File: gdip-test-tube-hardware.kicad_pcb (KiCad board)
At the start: 2 copper layers, 76.2 x 58.5 mm, 68 parts, among them J1 USB_B, J2 USB_B, J3 Screw_Terminal_01x02, J6 Screw_Terminal_01x02, Q1 BC818, Q2 BC818, Q3 BC818, SW1 SW_Push, SW2 SW_Push, U1 ESP32-S3-WROOM-1-N16R2, U2 AMS1117-3.3, U3 CP2102N-Axx-xQFN28, U4 USBLC6-2SC6, U5 USBLC6-2SC6, U6 74LVC2G00, U7 HDSP-7401, U8 74AHC595

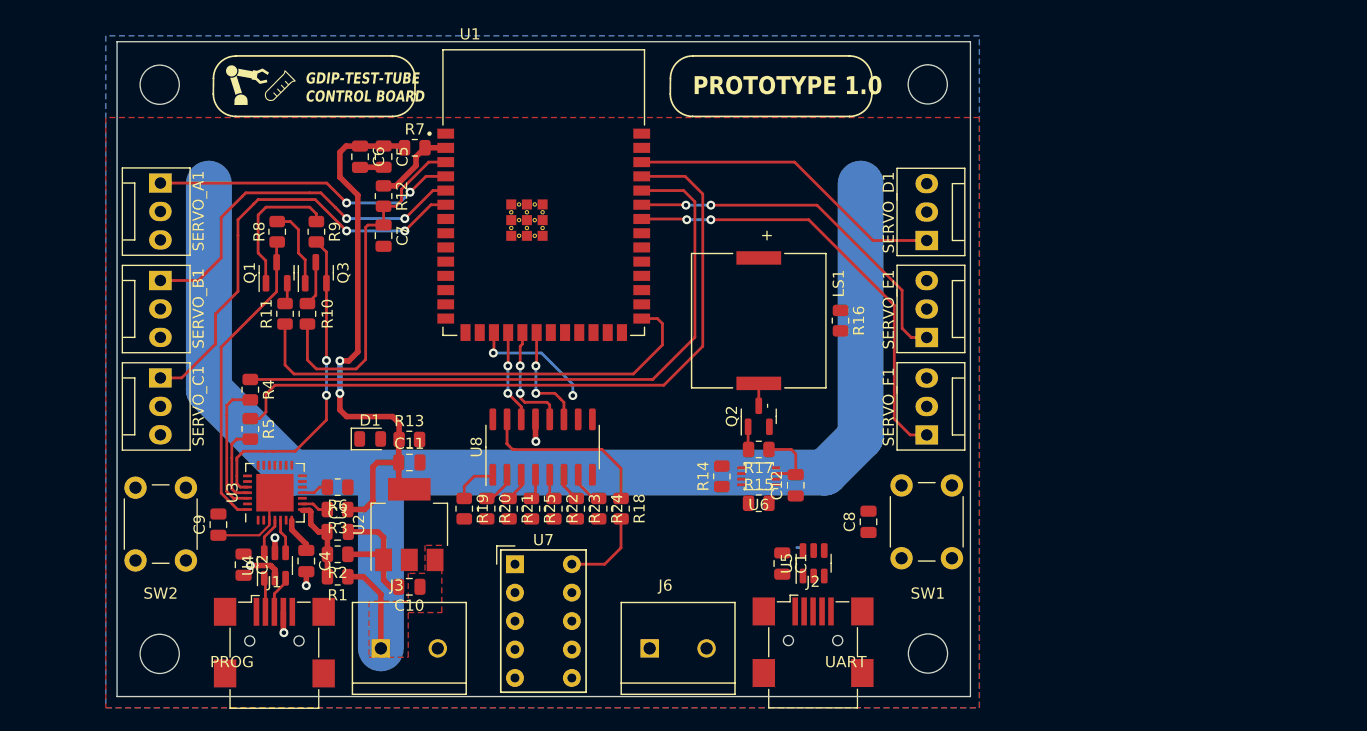
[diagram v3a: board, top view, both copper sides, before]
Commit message: Finished first layout added load switch for led saftey circuit,changed 47uF cap footprint. Also added extra pin headers for USB, Voltages & Gnd on board and extra GPIOs.
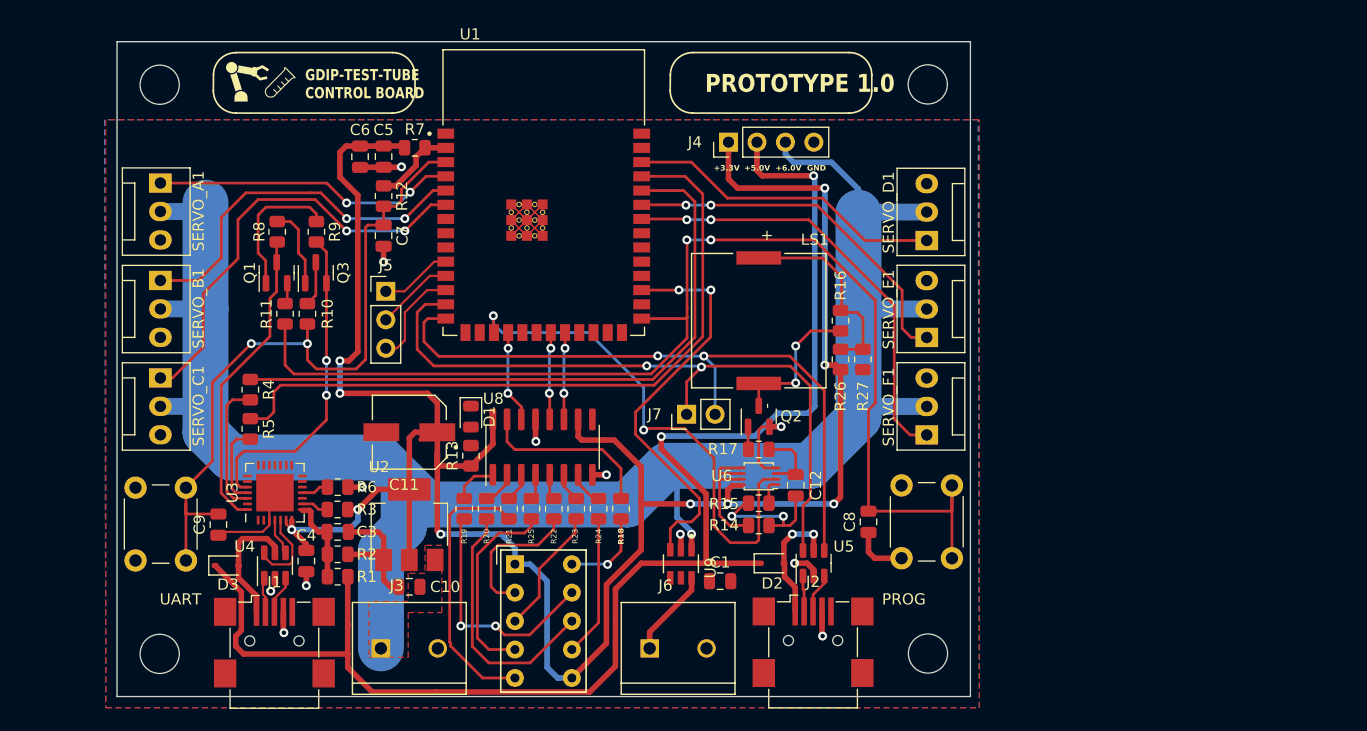
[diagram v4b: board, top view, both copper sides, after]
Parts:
- removed C2: 100nF, Capacitor_SMD:C_0805_2012Metric
- added D2: 1N5819WS, Diode_SMD:D_SOD-323, F.Cu at (158.5, 126.1)
- added D3: 1N5819WS, Diode_SMD:D_SOD-323, F.Cu at (109.8, 126.3)
- added J4: Conn_01x04, Connector_PinHeader_2.54mm:PinHeader_1x04_P2.54mm_Vertical, F.Cu at (154.6, 88.5)
- added J5: Conn_01x03, Connector_PinHeader_2.54mm:PinHeader_1x03_P2.54mm_Vertical, F.Cu at (124.0, 101.8)
- added J7: Conn_01x02, Connector_PinHeader_2.54mm:PinHeader_1x02_P2.54mm_Vertical, F.Cu at (150.9, 112.8)
- added R26: 4.7k, Resistor_SMD:R_0805_2012Metric, F.Cu at (164.6, 107.9)
- added R27: 3.9k, Resistor_SMD:R_0805_2012Metric, F.Cu at (166.6, 107.9)
- added U9: TPS22810DBVT, gdip-test-tube:SOT95P280X145-6N, F.Cu at (150.3, 126.1)
- C1: value 100nF -> 1uF
- C11: footprint Capacitor_SMD:C_0805_2012Metric -> gdip-test-tube:CAP_EEEHA1H470XP
- D1: value LED -> MCUPWR
- moved D1 9.22 mm to (131.6, 113.0), turned to -90 degrees
- moved C1 5.77 mm to (153.8, 127.7), turned to 0 degrees
- moved R13 5.69 mm to (131.6, 116.5), turned to 90 degrees
- moved R14 5.49 mm to (157.3, 122.7), turned to 180 degrees
- moved C11 2.70 mm to (126.1, 114.4), turned to 180 degrees
- moved G*** 0.30 mm to (114.2, 83.1)
- moved G*** 0.30 mm to (111.6, 83.1)
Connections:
- C1 pad 1: +5V -> Net-(J6-Pin_1)
- C10 pad 1: +5V -> +6V
- J1 pad 1: +5V -> Net-(D3-A)
- J2 pad 1: +5V -> Net-(D2-A)
- J3 pad 1: +5V -> +6V
- J6 pad 1: unconnected-(J6-Pin_1-Pad1) -> Net-(J6-Pin_1)
- J6 pad 2: unconnected-(J6-Pin_2-Pad2) -> GND
- SERVO_A1 pad 2: +5V -> +6V
- SERVO_B1 pad 2: +5V -> +6V
- SERVO_C1 pad 2: +5V -> +6V
- SERVO_D1 pad 2: +5V -> +6V
- SERVO_E1 pad 2: +5V -> +6V
- SERVO_F1 pad 2: +5V -> +6V
- U1 pad 10: unconnected-(U1-IO17-Pad10) -> /GPIO_EXTRA_1
- U1 pad 11: unconnected-(U1-IO18-Pad11) -> /GPIO_EXTRA_2
- U1 pad 12: unconnected-(U1-IO8-Pad12) -> /GPIO_EXTRA_3
- U1 pad 13: unconnected-(U1-IO19-Pad13) -> /D2-_OUT
- U1 pad 14: unconnected-(U1-IO20-Pad14) -> /D2+_OUT
- U1 pad 19: /GPIO_SR_RCLK -> unconnected-(U1-IO11-Pad19)
- U1 pad 20: /GPIO_SR_CLOCK -> unconnected-(U1-IO12-Pad20)
- U1 pad 21: unconnected-(U1-IO13-Pad21) -> /GPIO_SR_RCLK
- U1 pad 22: unconnected-(U1-IO14-Pad22) -> /GPIO_SR_CLOCK
- U1 pad 29: unconnected-(U1-IO36-Pad29) -> /GPIO_LED_SWITCH
- U2 pad 3: +5V -> +6V
- U4 pad 1: /D1+_IN -> /D1-_IN
- U4 pad 3: /D1-_IN -> /D1+_IN
- U4 pad 4: /D1-_OUT -> /D1+_OUT
- U4 pad 5: +5V -> Net-(D3-A)
- U4 pad 6: /D1+_OUT -> /D1-_OUT
- U5 pad 5: +5V -> Net-(D2-A)
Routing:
- net +6V: track 0.00 -> 169.6 mm, vias 0 -> 1
- net +3.3V: track 54.3 -> 206.1 mm, vias 2 -> 10
- net /GPIO0: track 42.7 -> 108.5 mm, vias 0 -> 2
- net /D2-_OUT: track 0.00 -> 62.4 mm, vias 0 -> 2
- net /D2+_OUT: track 0.00 -> 61.3 mm, vias 0 -> 2
- net GND: track 30.5 -> 68.0 mm, vias 4 -> 12
- net /GPIO_LED_SWITCH: track 0.00 -> 36.4 mm, vias 0 -> 2
- net /PWM6: track 11.1 -> 46.8 mm
- net /CHIP_PU: track 32.0 -> 62.6 mm, vias 0 -> 2
- net Net-(U7-D): track 0.00 -> 24.6 mm
- net Net-(U7-C): track 0.00 -> 23.0 mm
- net Net-(U7-B): track 0.00 -> 21.5 mm, vias 0 -> 2
- net +1V5: track 0.00 -> 18.2 mm
- net Net-(U7-E): track 0.00 -> 17.8 mm
- net Net-(R14-Pad2): track 0.00 -> 13.0 mm
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- added copper zone on F.Cu, net +6V
- removed copper zone on F.Cu, net +5V
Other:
- board text added: "+3.3V"
- board text added: "+5.0V"
- board text added: "+6.0V"
- board text added: "GND"
